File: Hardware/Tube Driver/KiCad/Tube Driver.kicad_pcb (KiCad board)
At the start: 2 copper layers, 157.5 x 30.5 mm, 45 parts, among them J1 I/O, Q1 MMBT3904, Q2 STN2580, Q3 MMBT3904, Q4 MMBT3906, U1 NE555D

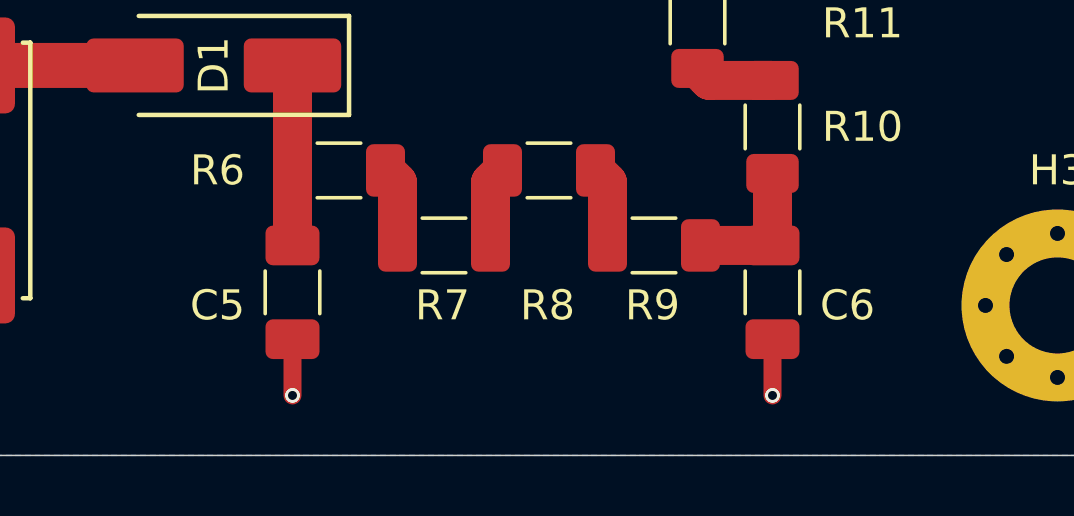
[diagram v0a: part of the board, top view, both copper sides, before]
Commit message: Added BoM, updated component values and PCB
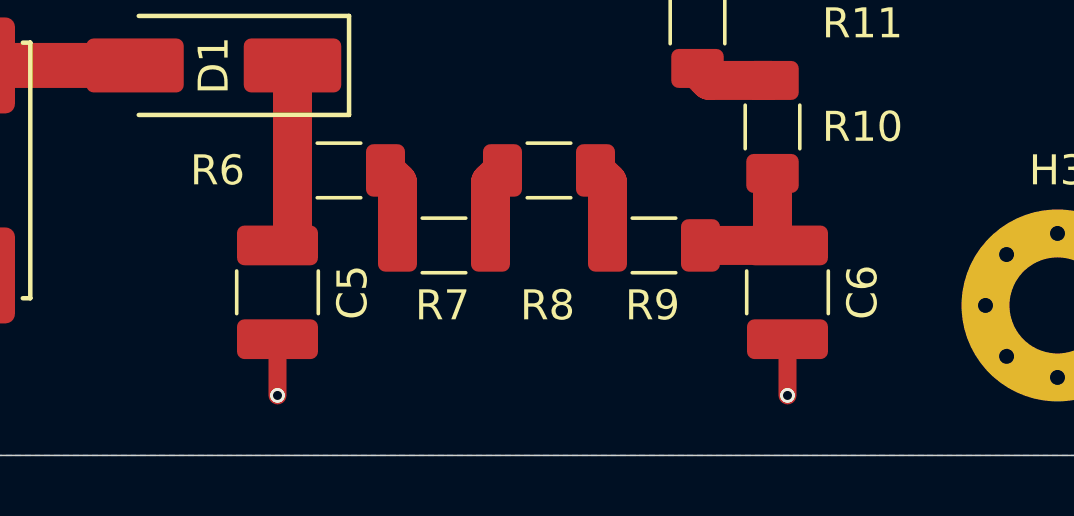
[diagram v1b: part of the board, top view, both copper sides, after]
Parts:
- C5, C6: value 50nF -> 47pF; footprint Capacitor_SMD:C_1206_3216Metric_Pad1.33x1.80mm_HandSolder -> Capacitor_SMD:C_1210_3225Metric_Pad1.33x2.70mm_HandSolder
- R6, R7, R8, R9: value 250k -> 240k
- moved C5 0.50 mm to (196.5, 115.6)
- moved C6 0.50 mm to (213.5, 115.6)
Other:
- board text added: ": Tube Driver : 1.0 : 2024-09-06"
- board text removed: ": Tube Driver : 1.0 : 2024-09-04"
